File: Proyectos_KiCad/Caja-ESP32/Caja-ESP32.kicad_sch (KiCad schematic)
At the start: 85 parts, among them J1 JACK_DC, J10 LOAD, J11 LOAD, J12 LOAD, J13 LOAD, J14 LOAD, J2 Fichero, J3 LOAD, J7 LOAD, J8 LOAD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

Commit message: Router
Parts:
- removed J11, J13, J9: LOAD, TerminalBlock_Phoenix:TerminalBlock_Phoenix_MKDS-1,5-2-5.08_1x02_P5.08mm_Horizontal, symbol Connector:Screw_Terminal_01x02
- R18, R19, R22, R23, R26, R27, R28, R29: footprint Resistor_THT:R_Axial_DIN0207_L6.3mm_D2.5mm_P15.24mm_Horizontal -> Resistor_THT:R_Axial_DIN0207_L6.3mm_D2.5mm_P10.16mm_Horizontal
- U6, U7, U8, U9: footprint Package_DIP:DIP-6_W7.62mm_LongPads -> @EmersonPrez15:MOC3020
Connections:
- net GND: now also U1.2 (IN-), U1.4 (-OUT); no longer U1. (-OUT)
- net RELE_1: now also U10.24 (CLK/GPIO18/D18); no longer U10.20 (TOUCH0/ADC2/GPIO4/D4)
- net RELE_2: now also U10.23 (CSO/GPIO5/D5); no longer U10.21 (UART2RX/GPIO16/D16)
- net RELE_4: now also U10.20 (TOUCH0/ADC2/GPIO4/D4); no longer U10.24 (CLK/GPIO18/D18)
- net VCC: now also U1.1 (IN+); no longer U1. (-OUT)
- net AC_1: now reaches Q5.2 (A2), R27.2, R29.2
- net AC_1: now also J7.2 (Pin_2), Q2.2 (A2), Q3.2 (A2), Q4.2 (A2), R18.2, R19.2, R22.2, R23.2, R26.2, R28.2
- net AC_2: now reaches J14.1 (Pin_1)
- net AC_2: now also J10.1 (Pin_1), J12.1 (Pin_1), J7.1 (Pin_1), J8.1 (Pin_1)
- net at D9.2 (A): now also U1.3 (+OUT); no longer U1. (-OUT)
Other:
- moved on the sheet: J7, J8

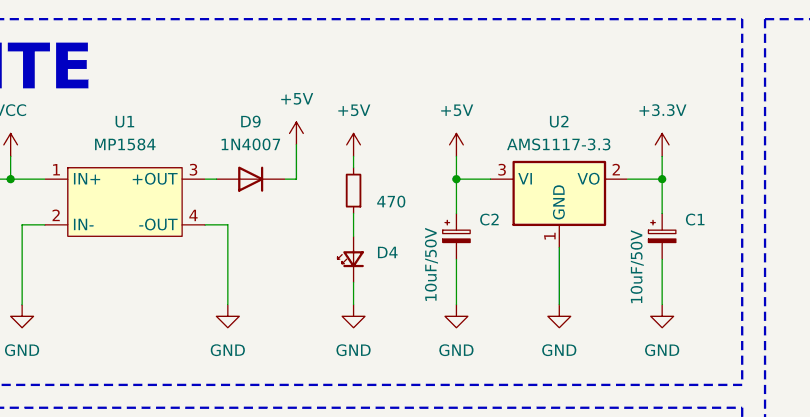
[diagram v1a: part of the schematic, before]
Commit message: Arreglando RAM
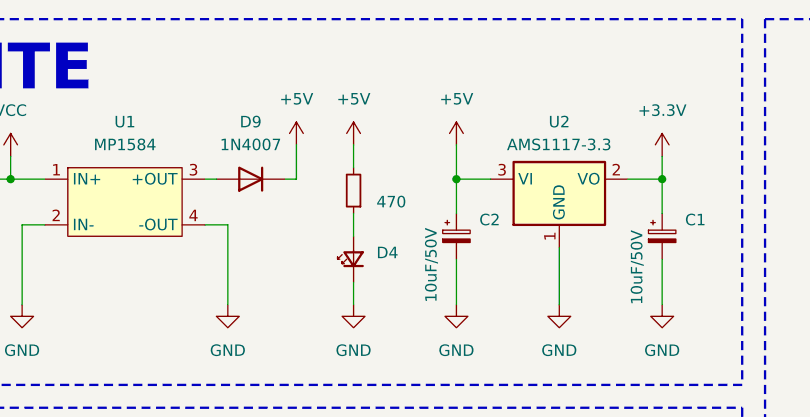
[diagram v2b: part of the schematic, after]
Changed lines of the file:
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@@
 	(wire
 		(pts
-			(xy 74.93 29.21) (xy 74.93 30.48)
+			(xy 74.93 27.94) (xy 74.93 30.48)
 		)
 		(stroke
@@
 	(wire
 		(pts
-			(xy 86.36 29.21) (xy 86.36 31.75)
+			(xy 86.36 27.94) (xy 86.36 31.75)
 		)
 		(stroke
@@
 	(symbol
 		(lib_id "power:+5V")
-		(at 74.93 29.21 0)
+		(at 74.93 27.94 0)
 		(unit 1)
 		(exclude_from_sim no)
@@
 		(fields_autoplaced yes)
 		(property "Reference" "#PWR039"
-			(at 74.93 33.02 0)
+			(at 74.93 31.75 0)
 			(effects
 				(font
@@
 		)
 		(property "Value" "+5V"
-			(at 74.93 24.13 0)
+			(at 74.93 22.86 0)
 			(effects
 				(font
@@
 		)
 		(property "Footprint" ""
-			(at 74.93 29.21 0)
+			(at 74.93 27.94 0)
 			(effects
 				(font
@@
 		)
 		(property "Datasheet" ""
-			(at 74.93 29.21 0)
+			(at 74.93 27.94 0)
 			(effects
 				(font
@@
 		)
 		(property "Description" "Power symbol creates a global label with name \"+5V\""
-			(at 74.93 29.21 0)
+			(at 74.93 27.94 0)
 			(effects
 				(font
@@
 	(symbol
 		(lib_id "power:+5V")
-		(at 86.36 29.21 0)
+		(at 86.36 27.94 0)
 		(unit 1)
 		(exclude_from_sim no)
@@
 		(fields_autoplaced yes)
 		(property "Reference" "#PWR04"
-			(at 86.36 33.02 0)
+			(at 86.36 31.75 0)
 			(effects
 				(font
@@
 		)
 		(property "Value" "+5V"
-			(at 86.36 24.13 0)
+			(at 86.36 22.86 0)
 			(effects
 				(font
@@
 		)
 		(property "Footprint" ""
-			(at 86.36 29.21 0)
+			(at 86.36 27.94 0)
 			(effects
 				(font
@@
 		)
 		(property "Datasheet" ""
-			(at 86.36 29.21 0)
+			(at 86.36 27.94 0)
 			(effects
 				(font
@@
 		)
 		(property "Description" "Power symbol creates a global label with name \"+5V\""
-			(at 86.36 29.21 0)
+			(at 86.36 27.94 0)
 			(effects
 				(font
